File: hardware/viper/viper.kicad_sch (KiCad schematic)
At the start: 57 parts, among them J1 TYPE-C-31-M-12, Q1 AO3400A, U1 ATmega32U4-M, U2 USBLC6-2SC6, Y1 16MHz

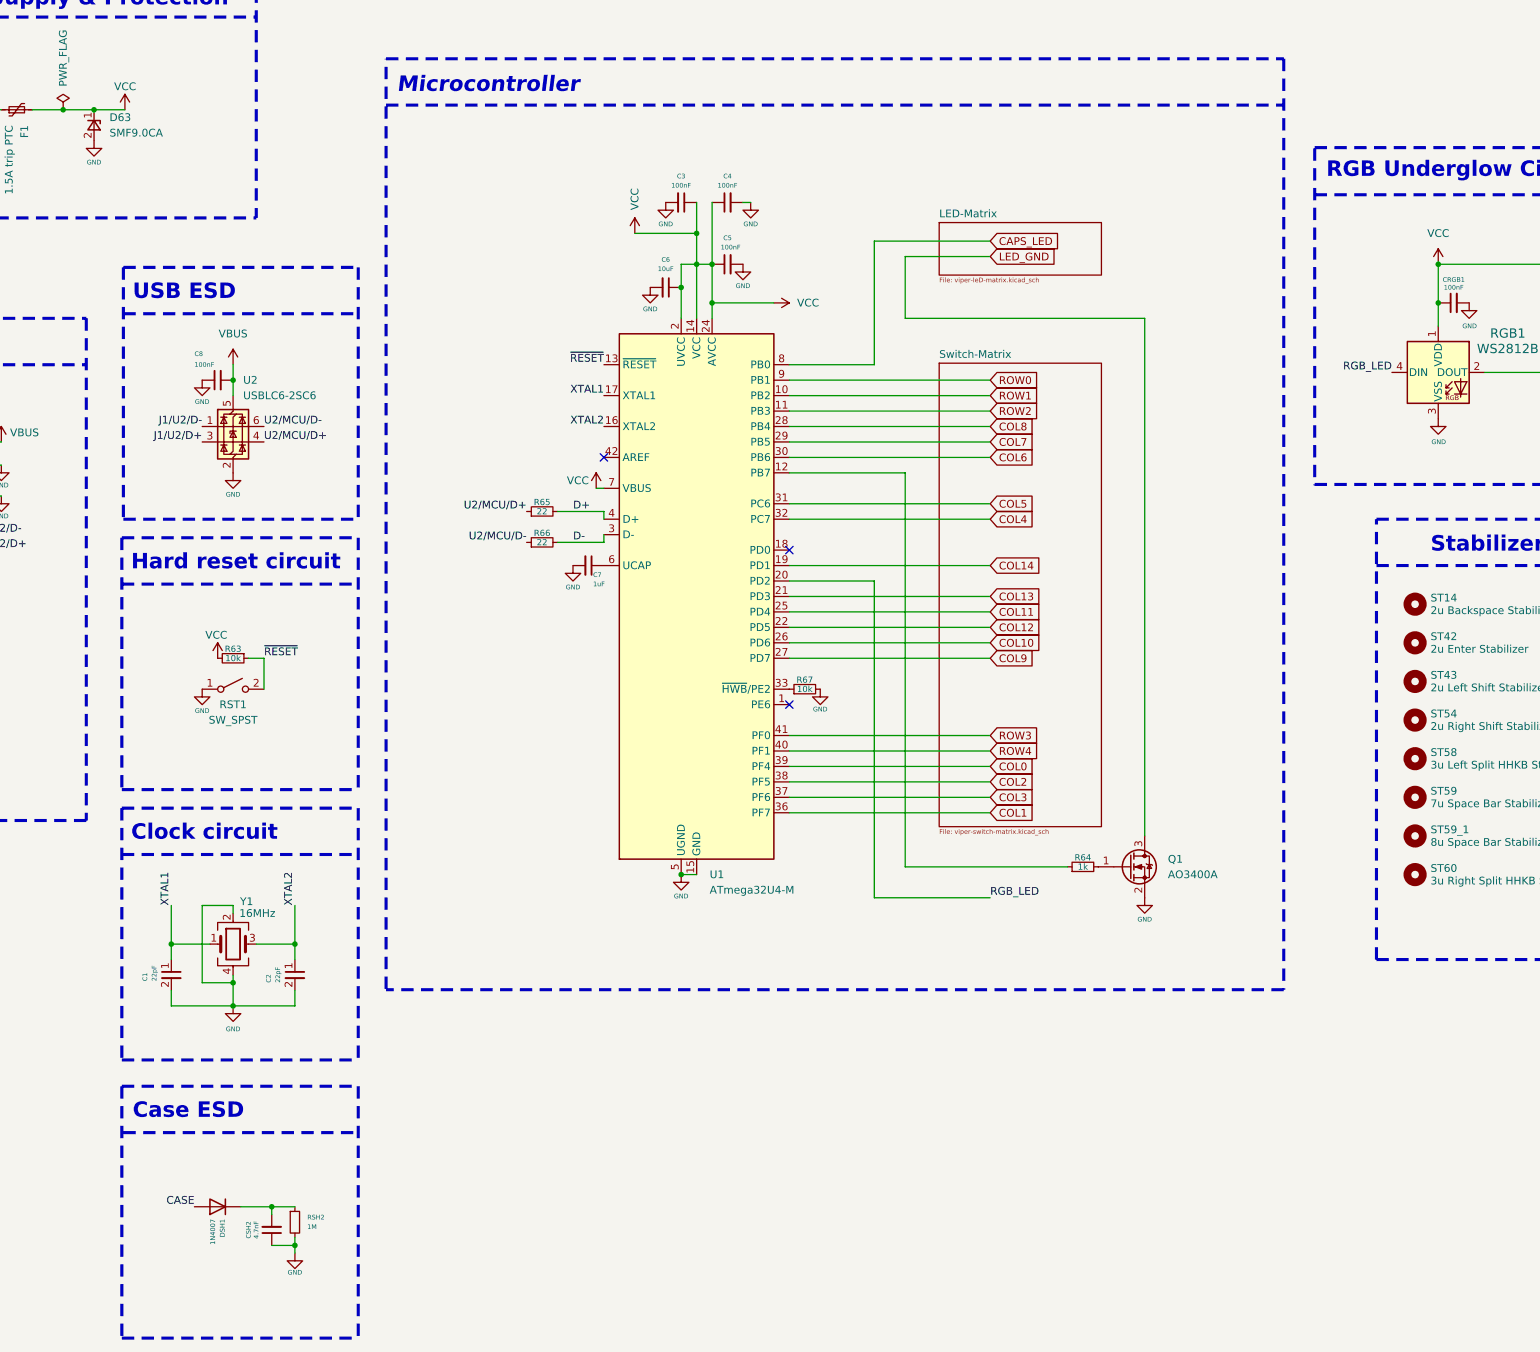
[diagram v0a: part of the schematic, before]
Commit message: Debugging footprints for cleaner DRC
Set soldermask properties & improved ref placement on back silkscreen

Silkscreen ref placement & forked HRO type-c receptacle due to edge cut

Flipping switches
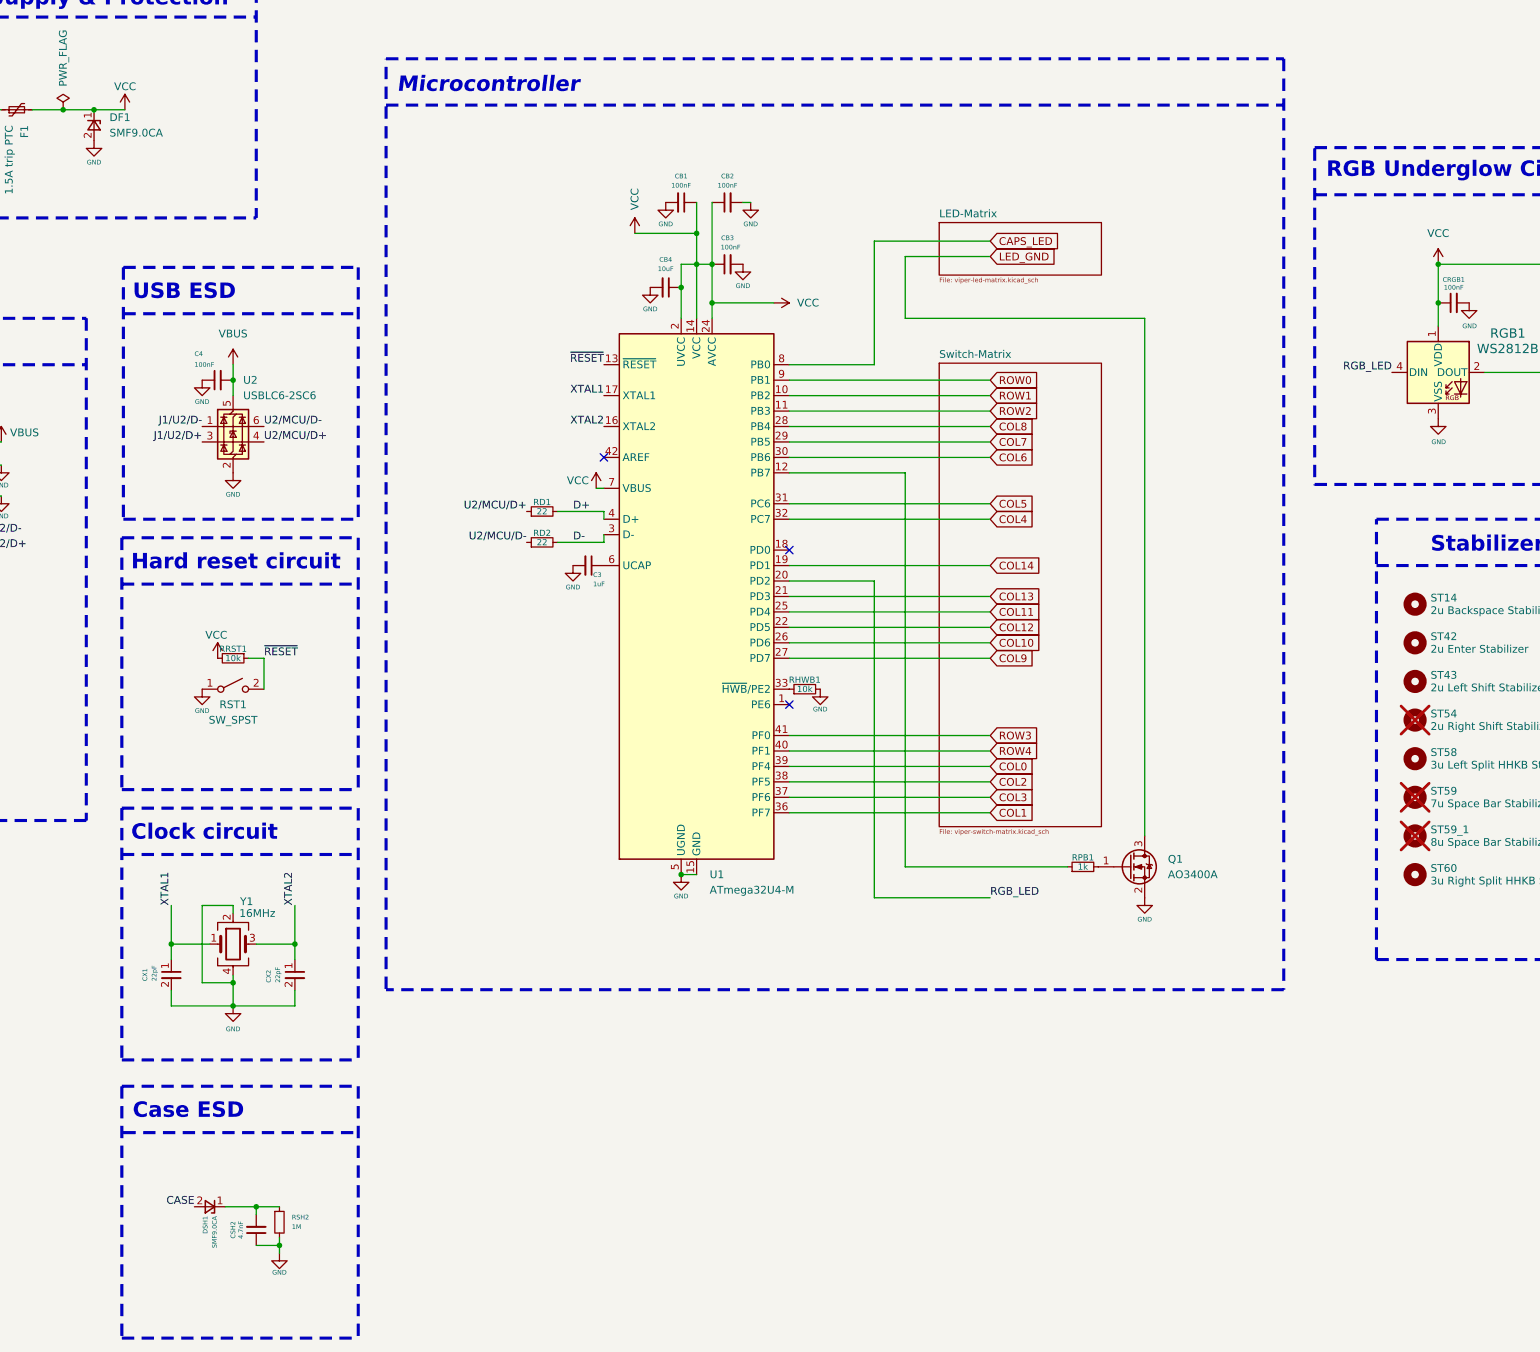
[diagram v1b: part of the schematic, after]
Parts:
- removed DSH1: 1N4007, Diode_SMD:D_SOD-123, symbol Device:D
- added DSH1: SMF9.0CA, Diode_SMD:D_SOD-123, symbol Device:D_Zener_Small
- J1: footprint Connector_USB:USB_C_Receptacle_HRO_TYPE-C-31-M-12 -> locallib:USB_C_Receptacle_HRO_TYPE-C-31-M-12
- RGB2: LCSC C5349955 -> C527089
- ST54, ST59, ST59_1: now not fitted
- renumbered C7 to C3, C8 to C4, C3 to CB1, C4 to CB2, C5 to CB3, C6 to CB4, C1 to CX1, C2 to CX2, D63 to DF1, R65 to RD1, R66 to RD2, R67 to RHWB1, R64 to RPB1, R63 to RRST1
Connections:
- net CASE: now also DSH1.2 (A)
- net at CSH2.2, RSH2.1: now also DSH1.1 (K)
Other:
- sheet LED-Matrix: file viper-leD-matrix.kicad_sch -> viper-led-matrix.kicad_sch
- moved on the sheet: CSH2, RSH2
